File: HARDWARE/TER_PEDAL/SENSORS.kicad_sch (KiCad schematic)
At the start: 11 parts, among them J2 APPS_1, J4 APPS_2, J5 BPPS_1, J6 SteerSensor

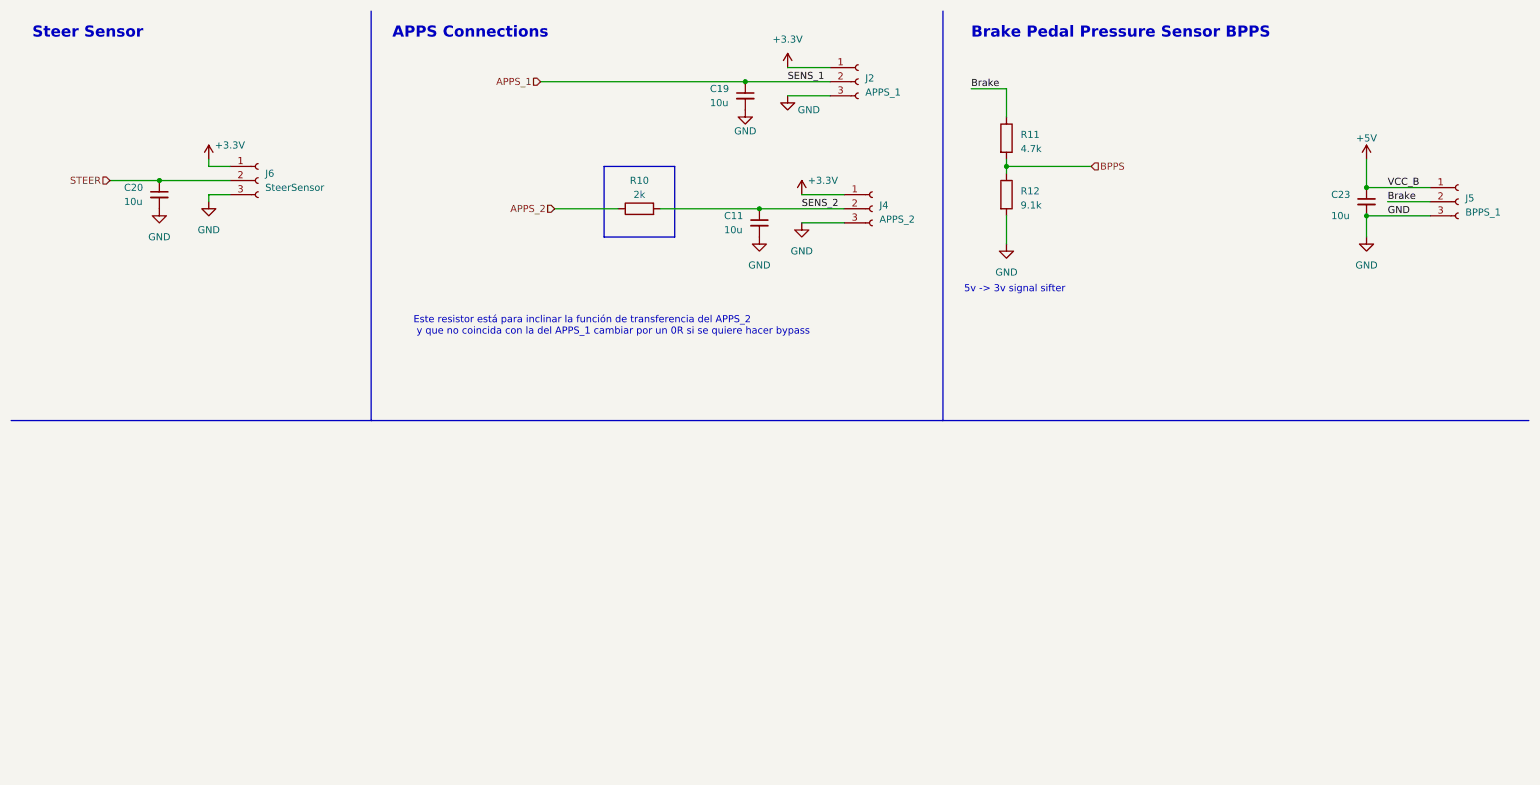
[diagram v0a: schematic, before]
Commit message: Added pull down resistors for adc to prevent floating value when disconnected signals, added LABELS lots of labels
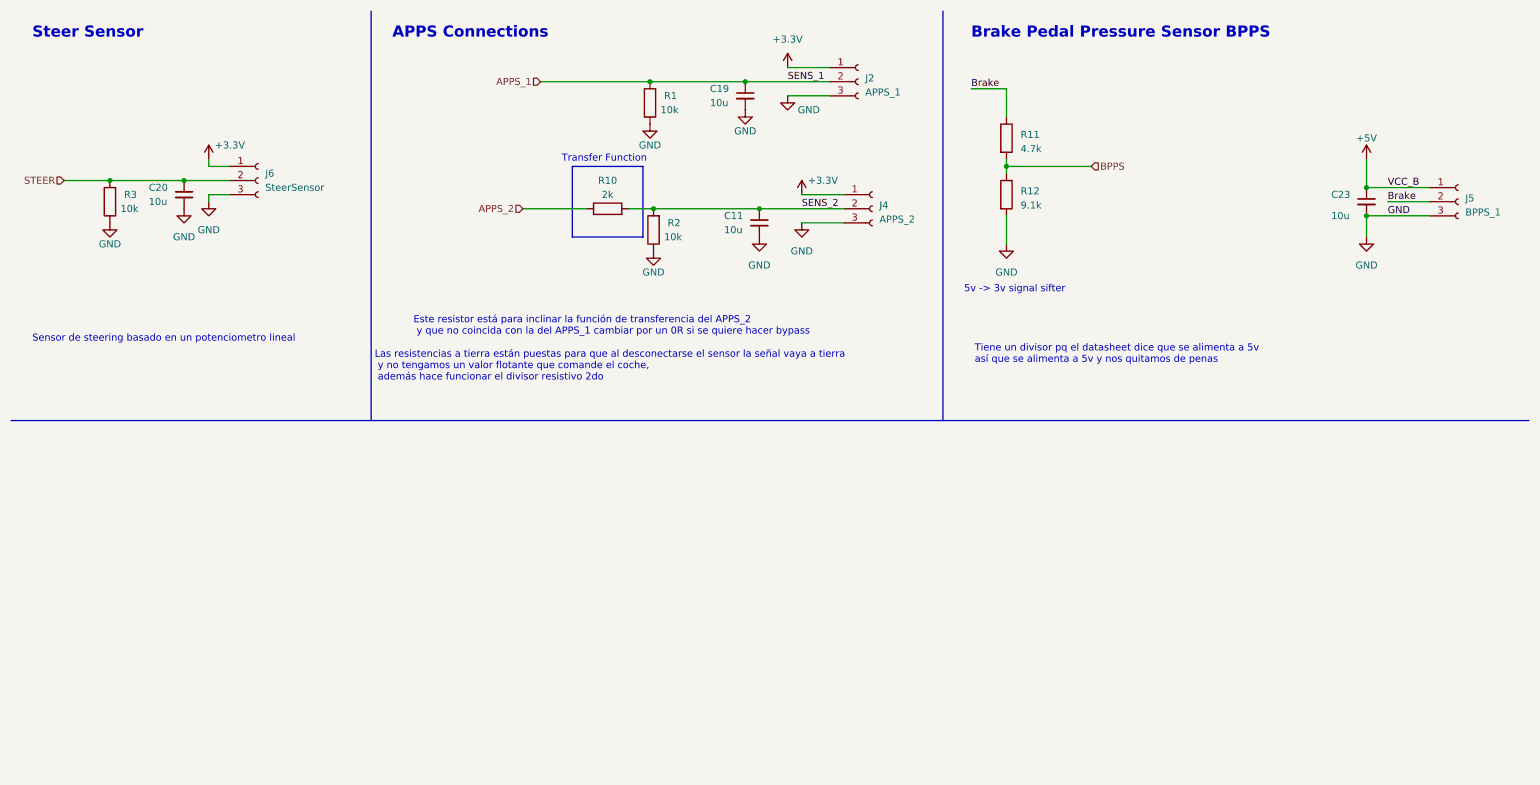
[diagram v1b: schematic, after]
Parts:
- added R1, R2, R3: 10k, Resistor_SMD:R_0603_1608Metric, symbol Device:R
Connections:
- net APPS_1: now also R1.2
- net GND: now also R1.1, R2.1, R3.1
- net SENS_2: now also R2.2
- net STEER: now also R3.2
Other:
- note added: "Las resistencias a tierra están puestas para que al desconectarse el sensor la señal vaya a tierra y no tengamos un valor flotante que comande el coche, además hace funcionar el divisor resistivo 2do"
- note added: "Sensor de steering basado en un potenciometro lineal"
- note added: "Tiene un divisor pq el datasheet dice que se alimenta a 5v así que se alimenta a 5v y nos quitamos de penas"
- note added: "Transfer Function"
- moved on the sheet: C20, R10

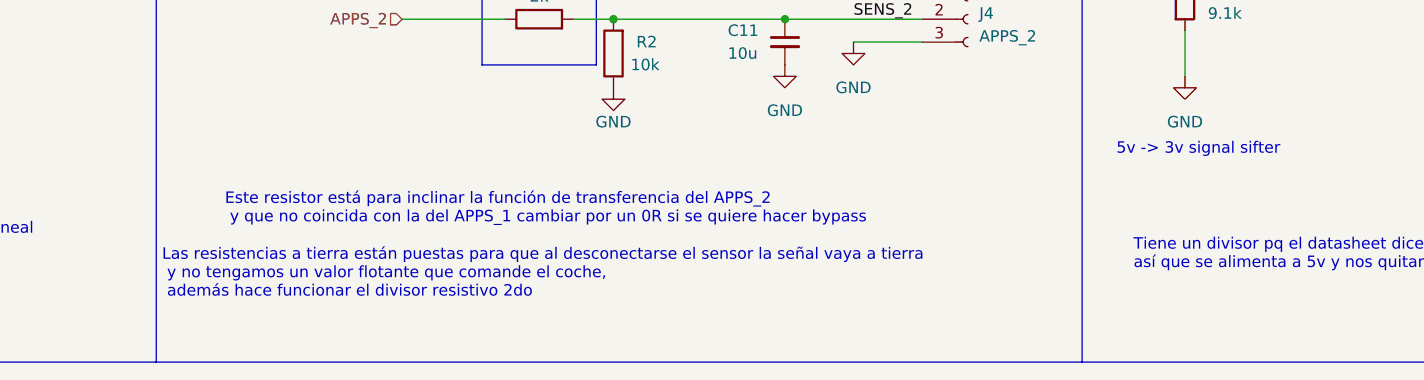
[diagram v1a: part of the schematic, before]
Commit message: Added Pulldown simulation
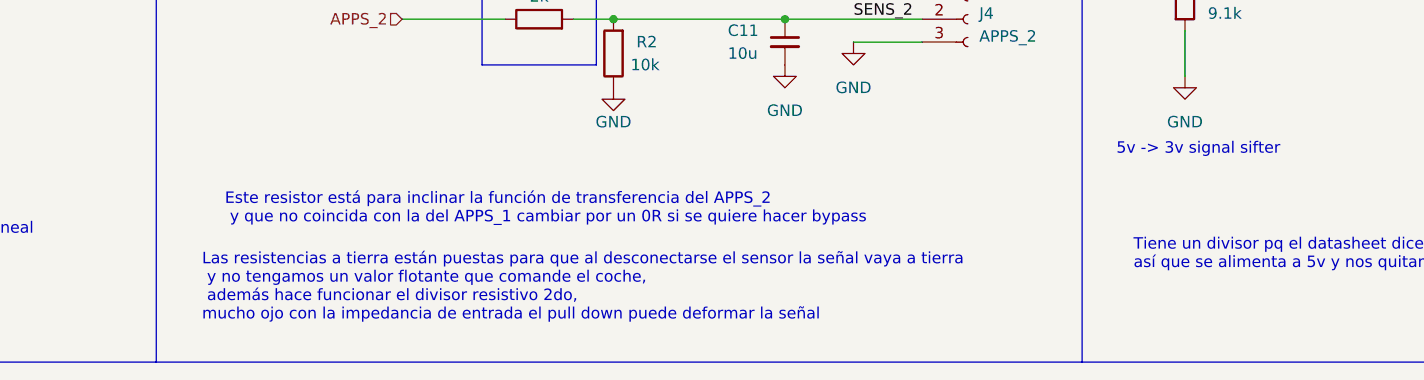
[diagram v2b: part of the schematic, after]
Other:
- note added: "Las resistencias a tierra están puestas para que al desconectarse el sensor la señal vaya a tierra y no tengamos un valor flotante que comande el coche, además hace funcionar el divisor resistivo 2do, mucho ojo con la impedancia de entrada el pull down puede deformar la señal"
- note removed: "Las resistencias a tierra están puestas para que al desconectarse el sensor la señal vaya a tierra y no tengamos un valor flotante que comande el coche, además hace funcionar el divisor resistivo 2do"
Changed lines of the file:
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@@
     (effects (font (size 1.27 1.27)) (justify left bottom))
   )
-  (text "Las resistencias a tierra están puestas para que al desconectarse el sensor la señal vaya a tierra\n y no tengamos un valor flotante que comande el coche,\n además hace funcionar el divisor resistivo 2do"
-    (at 76.835 79.375 0)
+  (text "Las resistencias a tierra están puestas para que al desconectarse el sensor la señal vaya a tierra\n y no tengamos un valor flotante que comande el coche,\n además hace funcionar el divisor resistivo 2do, \nmucho ojo con la impedancia de entrada el pull down puede deformar la señal"
+    (at 81.28 81.915 0)
     (effects (font (size 1.27 1.27)) (justify left bottom))
   )

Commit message: condensador señal brake
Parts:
- removed C23: 10u, Capacitor_SMD:C_0603_1608Metric, symbol Device:C_Small
- added C21: 390u, Capacitor_SMD:C_0603_1608Metric, symbol Device:C
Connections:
- net BPPS: now also C21.1
- net GND: now also C21.2

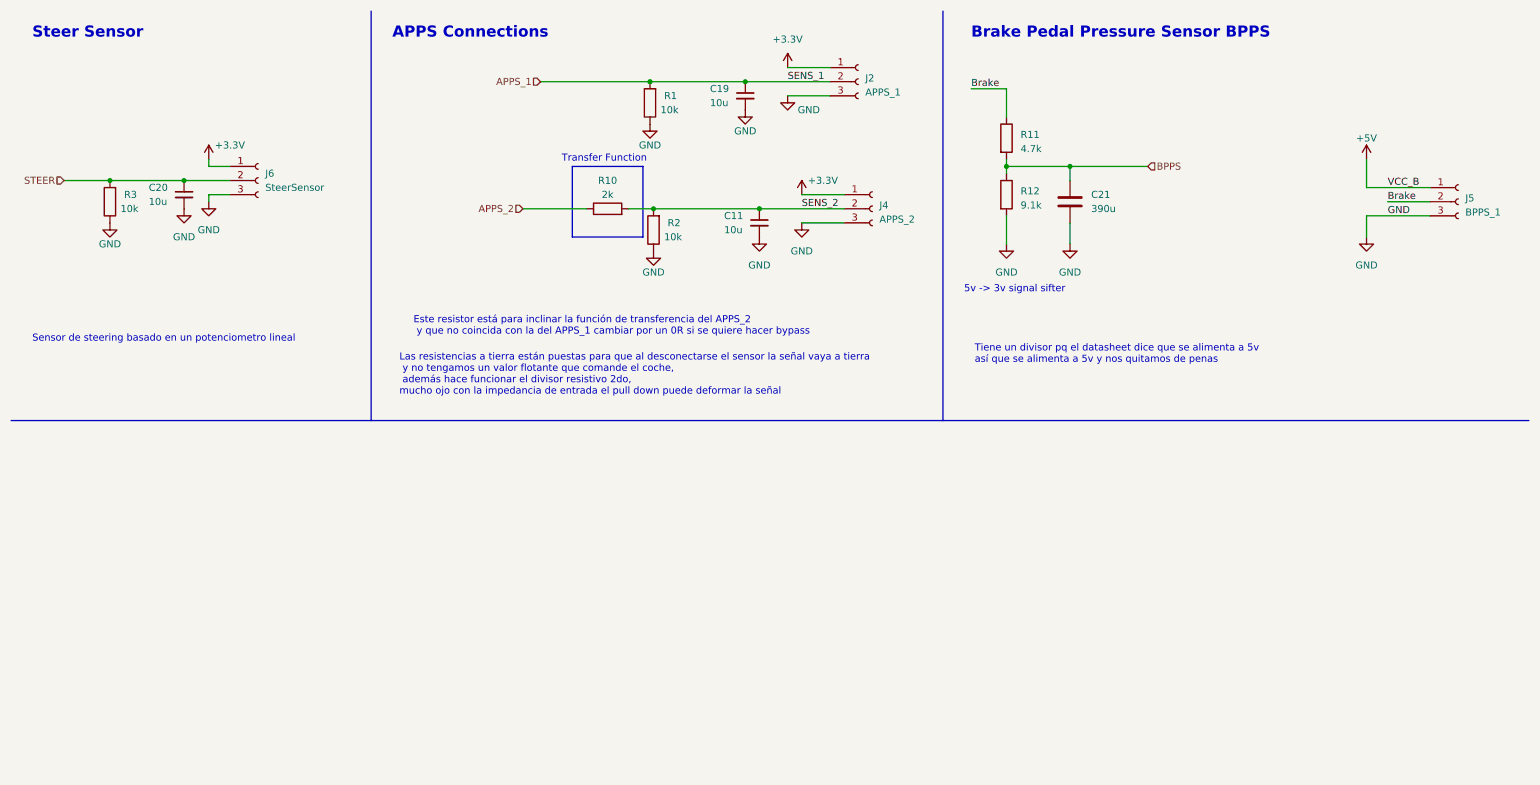
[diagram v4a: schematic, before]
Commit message: Added voltage followers to sensing, improved can circuitri, improved layout, waiting for routing
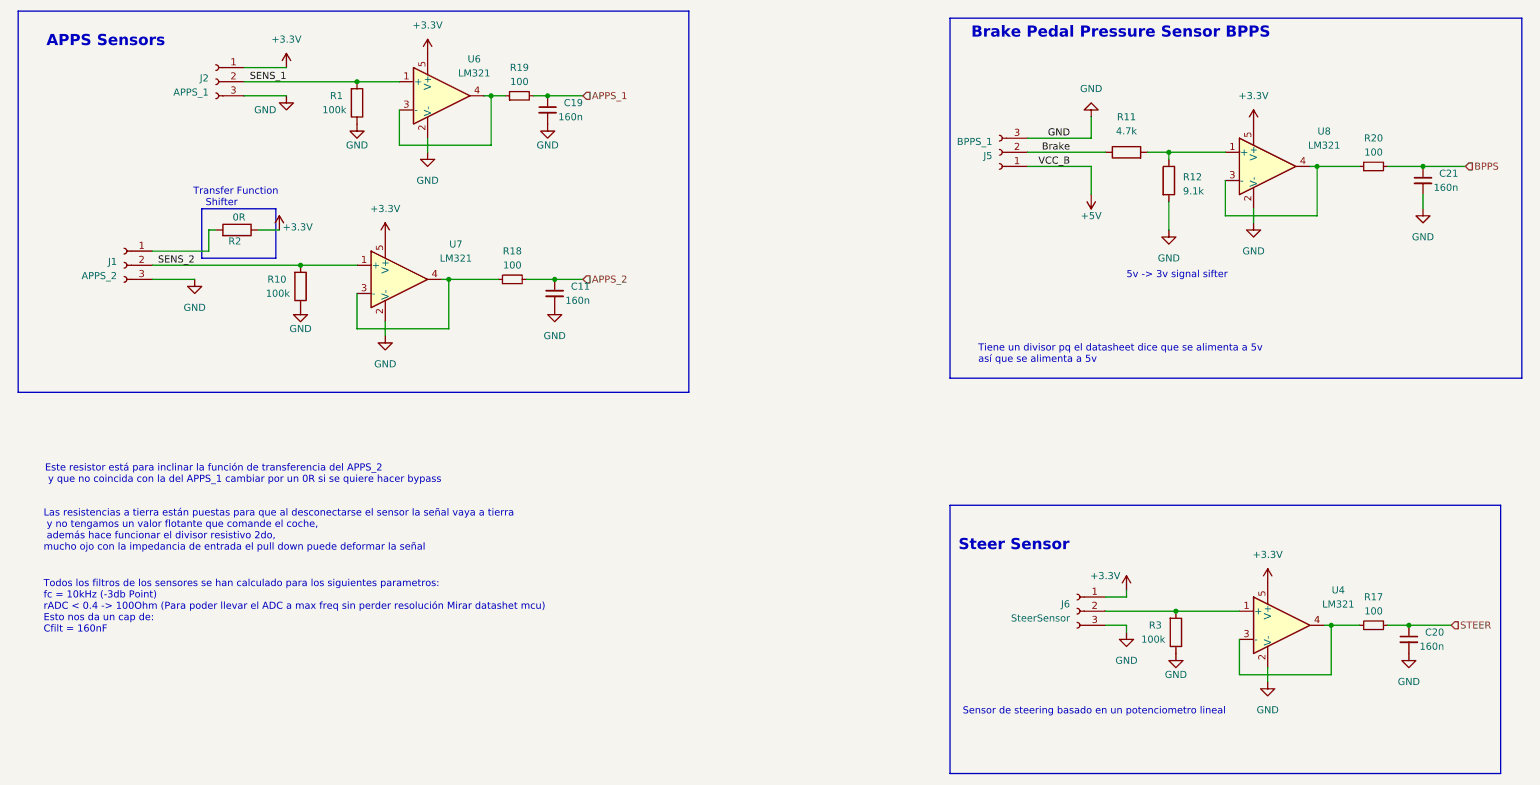
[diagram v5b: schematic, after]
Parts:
- removed C21: 390u, Capacitor_SMD:C_0603_1608Metric, symbol Device:C
- removed J4: APPS_2, Connector_JST:JST_PH_S3B-PH-K_1x03_P2.00mm_Horizontal, symbol Connector:Conn_01x03_Female
- added C21: 160n, Capacitor_SMD:C_0603_1608Metric, symbol Device:C_Small
- added J1: APPS_2, Connector_JST:JST_PH_S3B-PH-K_1x03_P2.00mm_Horizontal, symbol Connector:Conn_01x03_Female
- added R17, R18, R19, R20: 100, Resistor_SMD:R_0603_1608Metric, symbol Device:R_Small
- added U4, U6, U7, U8: LM321, Package_TO_SOT_SMD:SOT-23-5, symbol Amplifier_Operational:LM321
- C11, C19, C20: value 10u -> 160n
- R1, R3: value 10k -> 100k
- R10: value 2k -> 100k
- R2: value 10k -> 0R
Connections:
- net +3.3V: now also R2.1, U4.5 (V+), U6.5 (V+), U7.5 (V+), U8.5 (V+)
- net APPS_1: now also R19.2; no longer J2.2 (Pin_2), R1.2
- net APPS_2: now also C11.1, R18.2; no longer R10.1
- net BPPS: now also C21.1, R20.2; no longer R11.2, R12.1
- net GND: now also R10.1, C21.2, J1.3 (Pin_3), U4.2 (V-), U6.2 (V-), U7.2 (V-), U8.2 (V-); no longer R2.1
- net SENS_2: now also J1.2 (Pin_2), U7.1 (+); no longer C11.1, R2.2
- net STEER: now also R17.2; no longer J6.2 (Pin_2), R3.2
- new net: J6.2 (Pin_2), R3.2, U4.1 (+)
- new net: R18.1, U7.3 (-), U7.4
- new net: R19.1, U6.3 (-), U6.4
- new net: J1.1 (Pin_1), R2.2
- new net: R17.1, U4.3 (-), U4.4
- new net: R11.2, R12.1, U8.1 (+)
- new net: R20.1, U8.3 (-), U8.4
- new net SENS_1: J2.2 (Pin_2), R1.2, U6.1 (+)
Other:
- note added: "APPS Sensors"
- note added: "Tiene un divisor pq el datasheet dice que se alimenta a 5v así que se alimenta a 5v"
- note added: "Todos los filtros de los sensores se han calculado para los siguientes parametros: fc = 10kHz (-3db Point) rADC < 0.4 -> 100Ohm (Para poder llevar el ADC a max freq sin perder resolución Mirar datashet mcu) Esto nos da un cap de: Cfilt = 160nF"
- note added: "Transfer Function Shifter"
- note removed: "APPS Connections"
- note removed: "Tiene un divisor pq el datasheet dice que se alimenta a 5v así que se alimenta a 5v y nos quitamos de penas"
- note removed: "Transfer Function"
- company: (none) -> Tecnun-eRacing
- title: (none) -> TeR_PEDAL
- moved on the sheet: J2, J5, J6, R1, R11, R12, R3

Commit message: Alimentacion de los sensores de la apps actualizado a 5V
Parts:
- added R21, R22: 4.7k, Resistor_SMD:R_0603_1608Metric, symbol Device:R
- R1, R10: value 100k -> 9.1k
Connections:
- net +3.3V: no longer J2.1 (Pin_1), R2.1
- net +5V: now also J2.1 (Pin_1), R2.1
- net SENS_1: now also R21.2; no longer R1.2, U6.1 (+)
- net SENS_2: now also R22.2; no longer R10.2, U7.1 (+)
- new net: R1.2, R21.1, U6.1 (+)
- new net: R10.2, R22.1, U7.1 (+)
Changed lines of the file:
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@@
 	(wire
 		(pts
-			(xy 53.34 25.4) (xy 73.66 25.4)
+			(xy 53.34 25.4) (xy 62.23 25.4)
 		)
 		(stroke
@@
 	(wire
 		(pts
+			(xy 57.15 58.42) (xy 63.5 58.42)
+		)
+		(stroke
+			(width 0)
+			(type default)
+		)
+	)
+	(wire
+		(pts
 			(xy 46.99 52.07) (xy 48.26 52.07)
 		)
@@
 	(wire
 		(pts
-			(xy 36.83 58.42) (xy 63.5 58.42)
+			(xy 36.83 58.42) (xy 49.53 58.42)
 		)
 		(stroke
@@
 	(wire
 		(pts
+			(xy 69.85 25.4) (xy 73.66 25.4)
+		)
+		(stroke
+			(width 0)
+			(type default)
+		)
+	)
+	(wire
+		(pts
 			(xy 248.92 123.19) (xy 247.65 123.19)
 		)
@@
 			)
 		)
-		(property "Value" "+3.3V"
-			(at 60.96 17.78 0)
+		(property "Value" "+5V"
+			(at 63.5 21.5899 0)
 			(effects
 				(font
 					(size 1.27 1.27)
 				)
+				(justify right)
 			)
 		)
@@
 			)
 		)
-		(property "Value" "100k"
+		(property "Value" "9.1k"
 			(at 71.755 30.48 0)
 			(effects
@@
 	)
 	(symbol
+		(lib_id "Device:R")
+		(at 66.04 25.4 270)
+		(mirror x)
+		(unit 1)
+		(exclude_from_sim no)
+		(in_bom yes)
+		(on_board yes)
+		(dnp no)
+		(property "Reference" "R21"
+			(at 64.77 27.94 0)
+			(effects
+				(font
+					(size 1.27 1.27)
+				)
+				(justify right)
+			)
+		)
+		(property "Value" "4.7k"
+			(at 67.31 27.305 0)
+			(do_not_autoplace yes)
+			(effects
+				(font
+					(size 1.27 1.27)
+				)
+				(justify right)
+			)
+		)
+		(property "Footprint" "Resistor_SMD:R_0603_1608Metric"
+			(at 66.04 27.178 90)
+			(effects
+				(font
+					(size 1.27 1.27)
+				)
+				(hide yes)
+			)
+		)
+		(property "Datasheet" "~"
+			(at 66.04 25.4 0)
+			(effects
+				(font
+					(size 1.27 1.27)
+				)
+				(hide yes)
+			)
+		)
+		(property "Description" ""
+			(at 66.04 25.4 0)
+			(effects
+				(font
+					(size 1.27 1.27)
+				)
+				(hide yes)
+			)
+		)
+		(pin "1"
+		)
+		(pin "2"
+		)
+		(instances
+			(project "TER_PEDAL"
+				(path "/73ede3a3-6344-40fe-9207-10ff50d388ba/bd370b0f-91e5-4328-9d6f-8dc10ff0cff7"
+					(reference "R21")
+					(unit 1)
+				)
+			)
+		)
+	)
+	(symbol
 		(lib_id "Amplifier_Operational:LM321")
 		(at 88.9 27.94 0)
@@
 			)
 		)
-		(property "Value" "100k"
+		(property "Value" "9.1k"
 			(at 61.595 63.5 0)
 			(effects
@@
 			)
 		)
-		(property "Value" "+3.3V"
+		(property "Value" "+5V"
 			(at 62.992 51.562 0)
 			(effects
@@
 					(unit 1)
 				)
+			)
+		)
+	)
+	(symbol
+		(lib_id "Device:R")
+		(at 53.34 58.42 270)
+		(mirror x)
+		(unit 1)
+		(exclude_from_sim no)
+		(in_bom yes)
+		(on_board yes)
+		(dnp no)
+		(property "Reference" "R22"
+			(at 52.07 60.96 0)
+			(effects
+				(font
+					(size 1.27 1.27)
+				)
+				(justify right)
+			)
+		)
+		(property "Value" "4.7k"
+			(at 54.61 60.325 0)
+			(effects
+				(font
+					(size 1.27 1.27)
+				)
+				(justify right)
+			)
+		)
+		(property "Footprint" "Resistor_SMD:R_0603_1608Metric"
+			(at 53.34 60.198 90)
+			(effects
+				(font
+					(size 1.27 1.27)
+				)
+				(hide yes)
+			)
+		)
+		(property "Datasheet" "~"
+			(at 53.34 58.42 0)
+			(effects
+				(font
+					(size 1.27 1.27)
+				)
+				(hide yes)
+			)
+		)
+		(property "Description" ""
+			(at 53.34 58.42 0)
+			(effects
+				(font
+					(size 1.27 1.27)
+				)
+				(hide yes)
+			)
+		)
+		(pin "1"
+		)
+		(pin "2"
+		)
+		(instances
+			(project "TER_PEDAL"
+				(path "/73ede3a3-6344-40fe-9207-10ff50d388ba/bd370b0f-91e5-4328-9d6f-8dc10ff0cff7"
+					(reference "R22")
+					(unit 1)
+				)

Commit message: çMejorado layout
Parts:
- removed J6: SteerSensor, Connector_JST:JST_PH_S3B-PH-K_1x03_P2.00mm_Horizontal, symbol Connector:Conn_01x03_Female
- removed R17: 100, Resistor_SMD:R_0603_1608Metric, symbol Device:R_Small
- added J4: APPS_1, Connector_JST:JST_PH_S3B-PH-K_1x03_P2.00mm_Horizontal, symbol Connector:Conn_01x03_Female
- added R17: 9.1k, Resistor_SMD:R_0603_1608Metric, symbol Device:R
- added R23: 100, Resistor_SMD:R_0603_1608Metric, symbol Device:R_Small
- R3: value 100k -> 4.7k
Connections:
- net +5V: now also J4.1 (Pin_1)
- net GND: now also J4.3 (Pin_3), R17.1; no longer R3.1
- net STEER: now also R23.2
- net at U4.1 (+): now also R3.1, R17.2; no longer R3.2
- net at U4.3 (-), U4.4: now also R23.1
- new net: J4.2 (Pin_2), R3.2
